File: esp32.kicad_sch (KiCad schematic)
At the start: 15 parts, among them J2 Conn_01x05_Pin, Q3 MMBT3904, Q4 MMBT3904, U14 STM32F303RETx, Y1 ECS-2520MV-xxx-xx

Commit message: comit from pc
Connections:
- net GND: now also U1.57 (GND)
- net at U1.2 (VDD3P3): now also U1.3 (VDD3P3)
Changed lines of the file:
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@@
+	)
+	(symbol
+		(lib_id "power:GND")
+		(at 138.43 154.94 0)
+		(unit 1)
+		(exclude_from_sim no)
+		(in_bom yes)
+		(on_board yes)
+		(dnp no)
+		(fields_autoplaced yes)
+		(property "Reference" "#PWR77"
+			(at 138.43 161.29 0)
+			(effects
+				(font
+					(size 1.27 1.27)
+				)
+				(hide yes)
+			)
+		)
+		(property "Value" "GND"
+			(at 138.43 160.02 0)
+			(effects
+				(font
+					(size 1.27 1.27)
+				)
+			)
+		)
+		(property "Footprint" ""
+			(at 138.43 154.94 0)
+			(effects
+				(font
+					(size 1.27 1.27)
+				)
+				(hide yes)
+			)
+		)
+		(property "Datasheet" ""
+			(at 138.43 154.94 0)
+			(effects
+				(font
+					(size 1.27 1.27)
+				)
+				(hide yes)
+			)
+		)
+		(property "Description" "Power symbol creates a global label with name \"GND\" , ground"
+			(at 138.43 154.94 0)
+			(effects
+				(font
+					(size 1.27 1.27)
+				)
+				(hide yes)
+			)
+		)
+		(pin "1"
+		)
+		(instances
+			(project ""
+				(path "/c4754426-a41b-4341-9d09-2e389619f3d6"
+					(reference "#PWR77")
+					(unit 1)
+				)
+			)
+		)
 	)
 	(symbol

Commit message: aded an stmsheet to see the symbol
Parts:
- removed U14: STM32F303RETx, Package_QFP:LQFP-64_10x10mm_P0.5mm, symbol MCU_ST_STM32F3:STM32F303RETx
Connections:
- net at U1.2 (VDD3P3): now also U1.3 (VDD3P3)
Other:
- added sheet stm32 (stm32.sch.kicad_sch)
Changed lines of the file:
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@@
-	)
-	(symbol
-		(lib_id "MCU_ST_STM32F3:STM32F303RETx")
-		(at 261.62 102.87 0)
-		(unit 1)
-		(exclude_from_sim no)
-		(in_bom yes)
-		(on_board yes)
-		(dnp no)
-		(fields_autoplaced yes)
-		(property "Reference" "U14"
-			(at 266.3541 151.13 0)
-			(effects
-				(font
-					(size 1.27 1.27)
-				)
-				(justify left)
-			)
-		)
-		(property "Value" "STM32F303RETx"
-			(at 266.3541 153.67 0)
-			(effects
-				(font
-					(size 1.27 1.27)
-				)
-				(justify left)
-			)
-		)
-		(property "Footprint" "Package_QFP:LQFP-64_10x10mm_P0.5mm"
-			(at 246.38 148.59 0)
-			(effects
-				(font
-					(size 1.27 1.27)
-				)
-				(justify right)
-				(hide yes)
-			)
-		)
-		(property "Datasheet" "https://www.st.com/resource/en/datasheet/stm32f303re.pdf"
-			(at 261.62 102.87 0)
-			(effects
-				(font
-					(size 1.27 1.27)
-				)
-				(hide yes)
-			)
-		)
-		(property "Description" "STMicroelectronics Arm Cortex-M4 MCU, 512KB flash, 80KB RAM, 72 MHz, 2.0-3.6V, 51 GPIO, LQFP64"
-			(at 261.62 102.87 0)
-			(effects
-				(font
-					(size 1.27 1.27)
-				)
-				(hide yes)
-			)
-		)
-		(pin "59"
-		)
-		(pin "55"
-		)
-		(pin "57"
-		)
-		(pin "58"
-		)
-		(pin "6"
-		)
-		(pin "60"
-		)
-		(pin "61"
-		)
-		(pin "62"
-		)
-		(pin "63"
-		)
-		(pin "9"
-		)
-		(pin "64"
-		)
-		(pin "8"
-		)
-		(pin "56"
-		)
-		(pin "7"
-		)
-		(pin "24"
-		)
-		(pin "36"
-		)
-		(pin "50"
-		)
-		(pin "52"
-		)
-		(pin "37"
-		)
-		(pin "4"
-		)
-		(pin "40"
-		)
-		(pin "53"
-		)
-		(pin "22"
-		)
-		(pin "54"
-		)
-		(pin "46"
-		)
-		(pin "11"
-		)
-		(pin "12"
-		)
-		(pin "18"
-		)
-		(pin "14"
-		)
-		(pin "19"
-		)
-		(pin "2"
-		)
-		(pin "15"
-		)
-		(pin "28"
-		)
-		(pin "31"
-		)
-		(pin "32"
-		)
-		(pin "33"
-		)
-		(pin "34"
-		)
-		(pin "3"
-		)
-		(pin "13"
-		)
-		(pin "23"
-		)
-		(pin "30"
-		)
-		(pin "35"
-		)
-		(pin "49"
-		)
-		(pin "38"
-		)
-		(pin "1"
-		)
-		(pin "29"
-		)
-		(pin "25"
-		)
-		(pin "27"
-		)
-		(pin "26"
-		)
-		(pin "39"
-		)
-		(pin "16"
-		)
-		(pin "20"
-		)
-		(pin "41"
-		)
-		(pin "21"
-		)
-		(pin "42"
-		)
-		(pin "43"
-		)
-		(pin "44"
-		)
-		(pin "47"
-		)
-		(pin "17"
-		)
-		(pin "10"
-		)
-		(pin "45"
-		)
-		(pin "48"
-		)
-		(pin "5"
-		)
-		(pin "51"
-		)
-		(instances
-			(project ""
-				(path "/c4754426-a41b-4341-9d09-2e389619f3d6"
-					(reference "U14")
-					(unit 1)
-				)
-			)
-		)
 	)
 	(symbol
@@
 				)
 			)
+		)
+	)
+	(sheet
+		(at 180.34 27.94)
+		(size 27.94 20.32)
+		(fields_autoplaced yes)
+		(stroke
+			(width 0.1524)
+			(type solid)
+		)
+		(fill
+			(color 0 0 0 0.0000)
+		)
+		(property "Sheetname" "stm32"
+			(at 180.34 27.2284 0)
+			(effects
+				(font
+					(size 1.27 1.27)
+				)
+				(justify left bottom)
+			)
+		)
+		(property "Sheetfile" "stm32.sch.kicad_sch"
+			(at 180.34 48.8446 0)
+			(effects
+				(font
+					(size 1.27 1.27)
+				)
+				(justify left top)
+			)
+		)
+		(instances
+			(project "esp32"
+				(path "/c4754426-a41b-4341-9d09-2e389619f3d6"
+					(page "6")
+				)
+			)

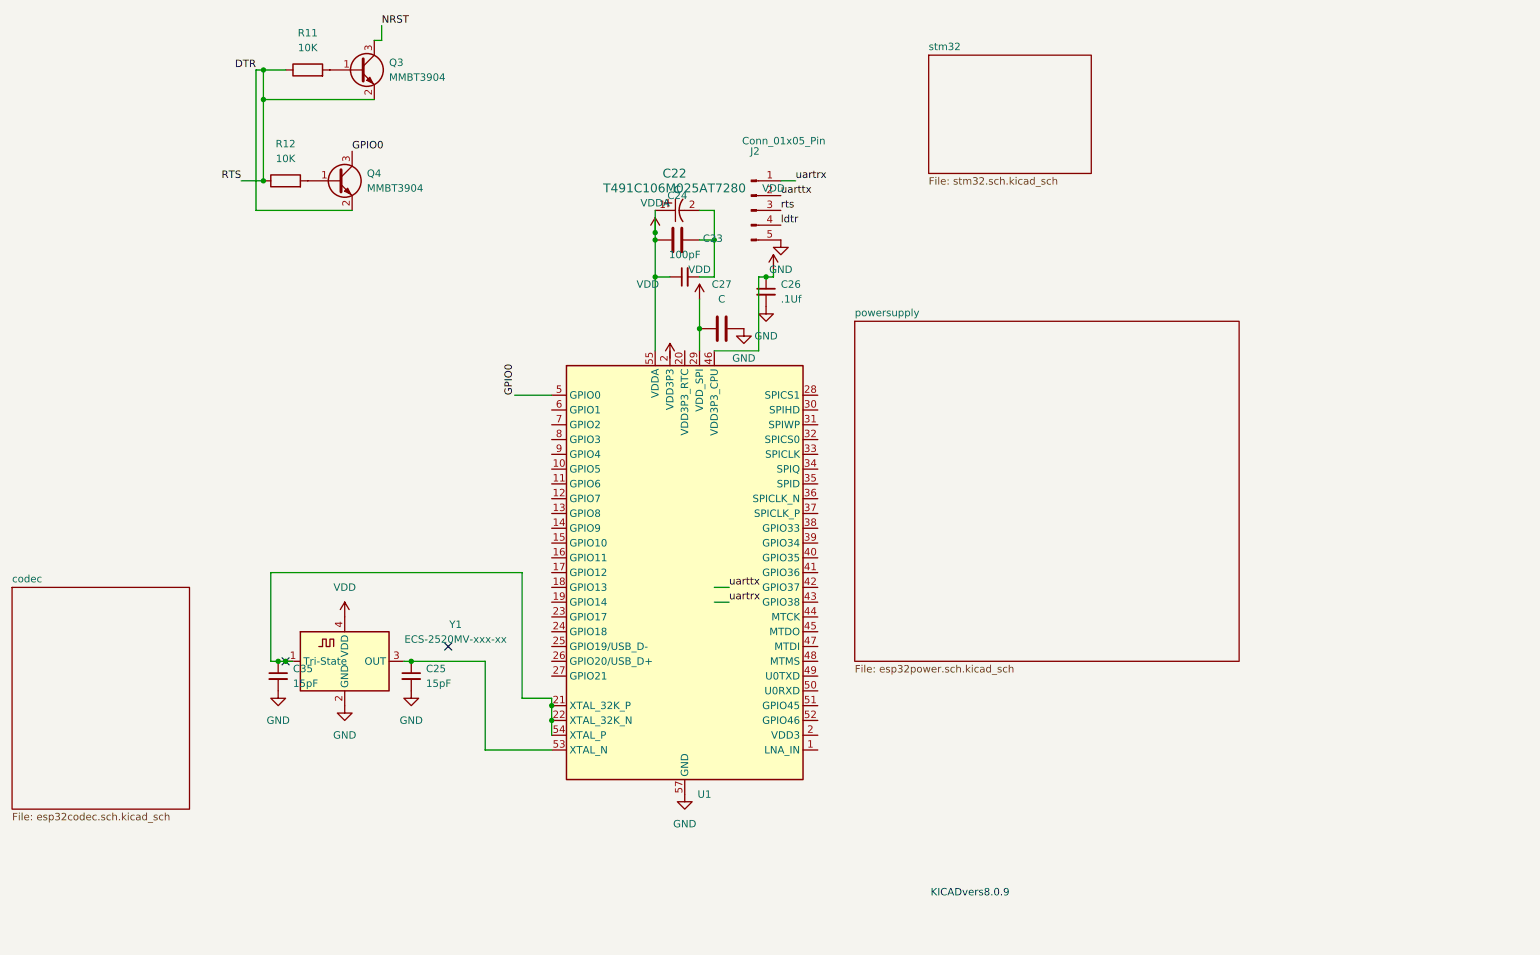
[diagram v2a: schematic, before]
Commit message: added pj398sm footprint to library
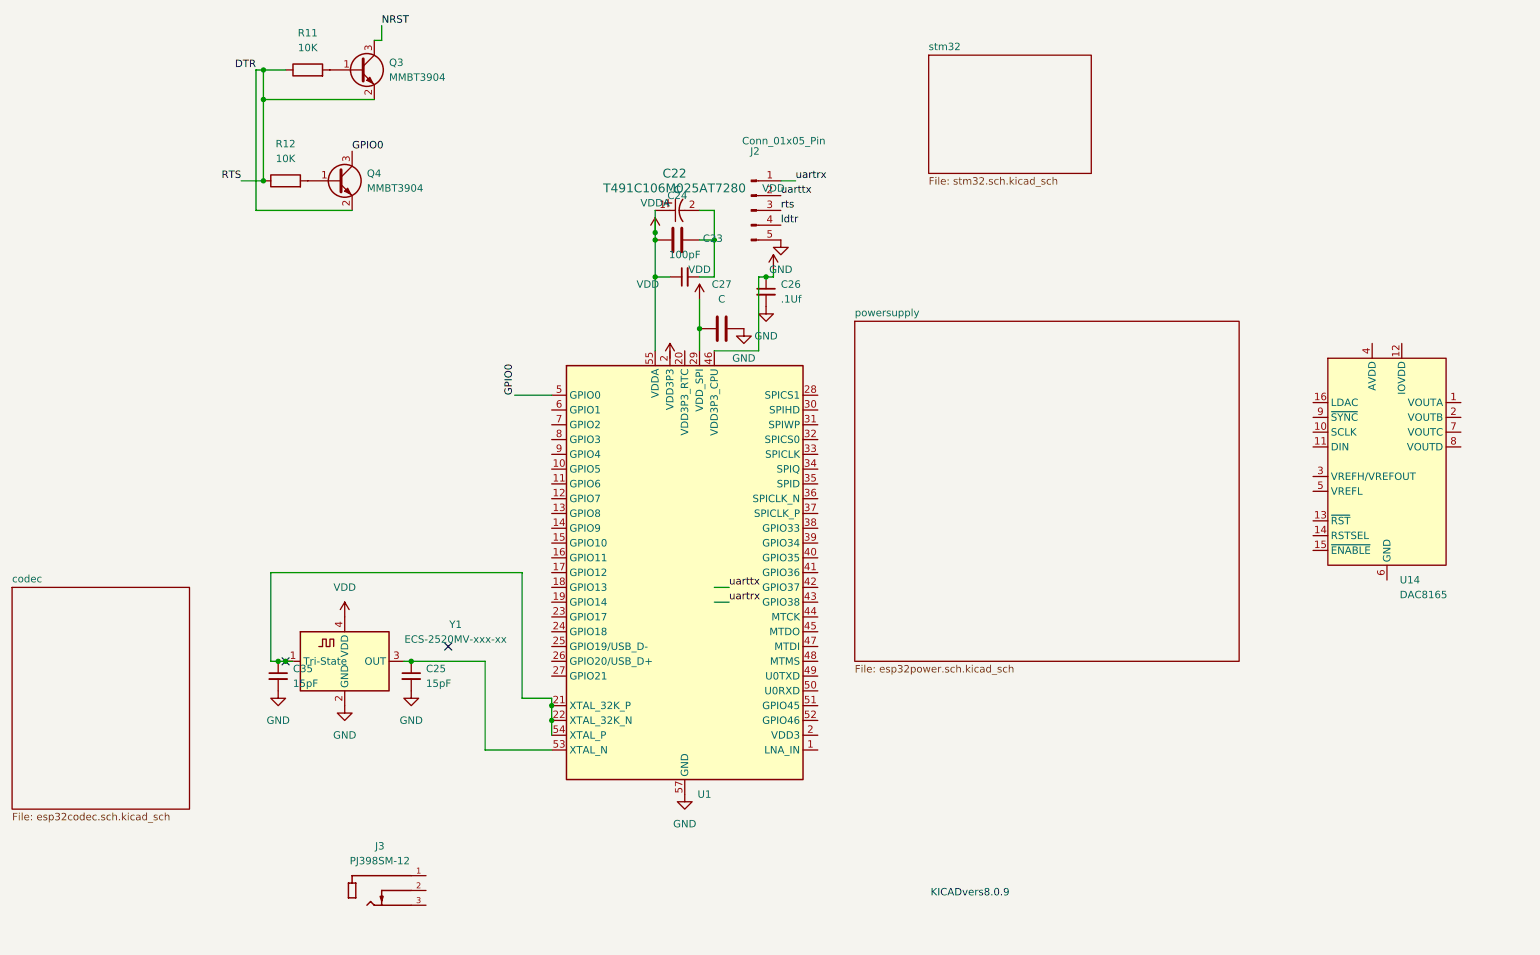
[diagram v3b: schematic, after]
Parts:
- added J3: PJ398SM-12, customfootprints:THONK_PJ398SM-12, symbol esp32lib:PJ398SM-12
- added U14: DAC8165, Package_SO:TSSOP-16_4.4x5mm_P0.65mm, symbol Analog_DAC:DAC8165
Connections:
- net at U1.2 (VDD3P3): now also U1.3 (VDD3P3)

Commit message: minor changes
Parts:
- removed U14: DAC8165, Package_SO:TSSOP-16_4.4x5mm_P0.65mm, symbol Analog_DAC:DAC8165
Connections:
- net uartrx: now also U1.49 (U0TXD)
- net at U1.2 (VDD3P3): now also U1.3 (VDD3P3)
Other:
- added sheet DAC (dac.sch.kicad_sch)
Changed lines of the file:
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@@
 	(wire
 		(pts
-			(xy 153.67 66.04) (xy 153.67 64.77)
-		)
-		(stroke
-			(width 0)
-			(type default)
-		)
-	)
-	(wire
-		(pts
-			(xy 146.05 121.92) (xy 143.51 121.92)
+			(xy 162.56 52.07) (xy 154.94 52.07)
+		)
+		(stroke
+			(width 0)
+			(type default)
+		)
+	)
+	(wire
+		(pts
+			(xy 162.56 66.04) (xy 162.56 64.77)
+		)
+		(stroke
+			(width 0)
+			(type default)
+		)
+	)
+	(wire
+		(pts
+			(xy 143.51 124.46) (xy 143.51 121.92)
 		)
 		(stroke
@@
 	(wire
 		(pts
+			(xy 165.1 134.62) (xy 161.29 134.62)
+		)
+		(stroke
+			(width 0)
+			(type default)
+		)
+	)
+	(wire
+		(pts
 			(xy 146.05 119.38) (xy 143.51 119.38)
 		)
@@
 	(wire
 		(pts
-			(xy 153.67 66.04) (xy 152.4 66.04)
+			(xy 162.56 66.04) (xy 152.4 66.04)
 		)
 		(stroke
@@
 	)
 	(label "uarttx"
-		(at 154.94 52.07 0)
-		(effects
-			(font
-				(size 1.27 1.27)
-			)
-			(justify left bottom)
-		)
-	)
-	(label "uarttx"
-		(at 146.05 119.38 0)
+		(at 162.56 52.07 0)
 		(effects
 			(font
@@
 		)
 	)
-	(label "uartrx"
-		(at 146.05 121.92 0)
+	(label "GPIO0"
+		(at 109.22 86.36 90)
 		(effects
 			(font
@@
 		)
 	)
-	(label "GPIO0"
-		(at 109.22 86.36 90)
+	(label "uartrx"
+		(at 165.1 134.62 0)
 		(effects
 			(font
@@
 	)
 	(symbol
-		(lib_id "Analog_DAC:DAC8165")
-		(at 259.08 100.33 0)
-		(unit 1)
-		(exclude_from_sim no)
-		(in_bom yes)
-		(on_board yes)
-		(dnp no)
-		(fields_autoplaced yes)
-		(property "Reference" "U14"
-			(at 261.2741 118.11 0)
-			(effects
-				(font
-					(size 1.27 1.27)
-				)
-				(justify left)
-			)
-		)
-		(property "Value" "DAC8165"
-			(at 261.2741 120.65 0)
-			(effects
-				(font
-					(size 1.27 1.27)
-				)
-				(justify left)
-			)
-		)
-		(property "Footprint" "Package_SO:TSSOP-16_4.4x5mm_P0.65mm"
-			(at 236.22 118.11 0)
-			(effects
-				(font
-					(size 1.27 1.27)
-				)
-				(hide yes)
-			)
-		)
-		(property "Datasheet" "https://www.ti.com/lit/ds/symlink/dac8165.pdf"
-			(at 233.68 118.11 0)
-			(effects
-				(font
-					(size 1.27 1.27)
-				)
-				(hide yes)
-			)
-		)
-		(property "Description" "14-bit quad-channel voltage output DAC with 2.5V internal reference"
-			(at 259.08 100.33 0)
-			(effects
-				(font
-					(size 1.27 1.27)
-				)
-				(hide yes)
-			)
-		)
-		(pin "4"
-		)
-		(pin "7"
-		)
-		(pin "8"
-		)
-		(pin "6"
-		)
-		(pin "13"
-		)
-		(pin "16"
-		)
-		(pin "14"
-		)
-		(pin "1"
-		)
-		(pin "10"
-		)
-		(pin "11"
-		)
-		(pin "12"
-		)
-		(pin "15"
-		)
-		(pin "2"
-		)
-		(pin "3"
-		)
-		(pin "5"
-		)
-		(pin "9"
-		)
-		(instances
-			(project ""
-				(path "/c4754426-a41b-4341-9d09-2e389619f3d6"
-					(reference "U14")
-					(unit 1)
-				)
-			)
-		)
-	)
-	(symbol
 		(lib_id "esp32lib:T491C106M025AT7280")
 		(at 133.35 54.61 0)
@@
 	(symbol
 		(lib_id "power:VDD")
-		(at 153.67 64.77 0)
+		(at 162.56 64.77 0)
 		(unit 1)
 		(exclude_from_sim no)
@@
 		(on_board yes)
 		(dnp no)
+		(fields_autoplaced yes)
 		(property "Reference" "#PWR59"
-			(at 153.67 68.58 0)
+			(at 162.56 68.58 0)
 			(effects
 				(font
@@
 		)
 		(property "Value" "VDD"
-			(at 153.67 50.8 0)
+			(at 162.56 59.69 0)
 			(effects
 				(font
@@
 		)
 		(property "Footprint" ""
-			(at 153.67 64.77 0)
+			(at 162.56 64.77 0)
 			(effects
 				(font
@@
 		)
 		(property "Datasheet" ""
-			(at 153.67 64.77 0)
+			(at 162.56 64.77 0)
 			(effects
 				(font
@@
 		)
 		(property "Description" "Power symbol creates a global label with name \"VDD\""
-			(at 153.67 64.77 0)
+			(at 162.56 64.77 0)
 			(effects
 				(font
@@
 				)
 			)
+		)
+	)
+	(sheet
+		(at 243.84 30.48)
+		(size 17.78 38.1)
+		(fields_autoplaced yes)
+		(stroke
+			(width 0.1524)
+			(type solid)
+		)
+		(fill
+			(color 0 0 0 0.0000)
+		)
+		(property "Sheetname" "DAC"
+			(at 243.84 29.7684 0)
+			(effects
+				(font
+					(size 1.27 1.27)
+				)
+				(justify left bottom)
+			)
+		)
+		(property "Sheetfile" "dac.sch.kicad_sch"
+			(at 243.84 69.1646 0)
+			(effects
+				(font
+					(size 1.27 1.27)
+				)
+				(justify left top)
+			)
+		)
+		(instances
+			(project "esp32"
+				(path "/c4754426-a41b-4341-9d09-2e389619f3d6"
+					(page "7")
+				)
+			)
